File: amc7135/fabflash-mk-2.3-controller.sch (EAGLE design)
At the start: 6 parts, among them U1 Tiny85

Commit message: slowly making progress toward a buildable device
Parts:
- added JP3, JP4, JP5, JP6: M01PTH-0.9MM-NS, A_butts:M01PTH-0.9MM-NS
- JP1, JP2: value (none) -> M01PTH-0.9MM-NS; device A_butts:M05PTH -> A_butts:M01PTH-0.9MM-NS
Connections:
- net 5V: now also JP6.1; no longer JP1.4, JP2.4
- net BLUEPWM: now also JP4.1; no longer JP1.2
- net GND: now also JP3.1; no longer JP1.1, JP1.5, JP2.1, JP2.5
- net GREENPWM: now also JP1.1; no longer JP2.2
- net REDPWM: now also JP2.1; no longer JP2.3
- net WHITEPWM: now also JP5.1; no longer JP1.3
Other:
- moved on the sheet: C1, R1, S1, U1

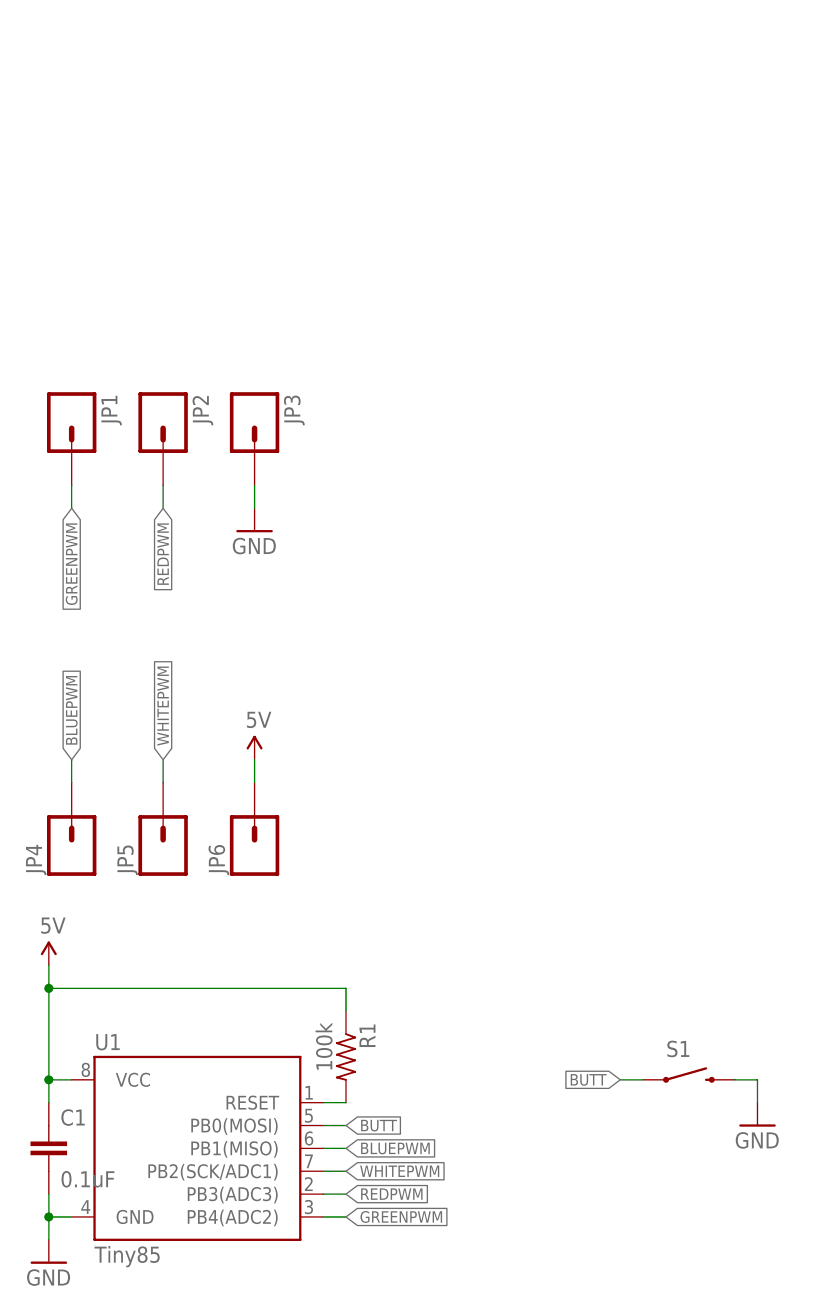
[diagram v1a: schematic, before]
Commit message: batt con plate to smd, controller with isp using jst-zh con
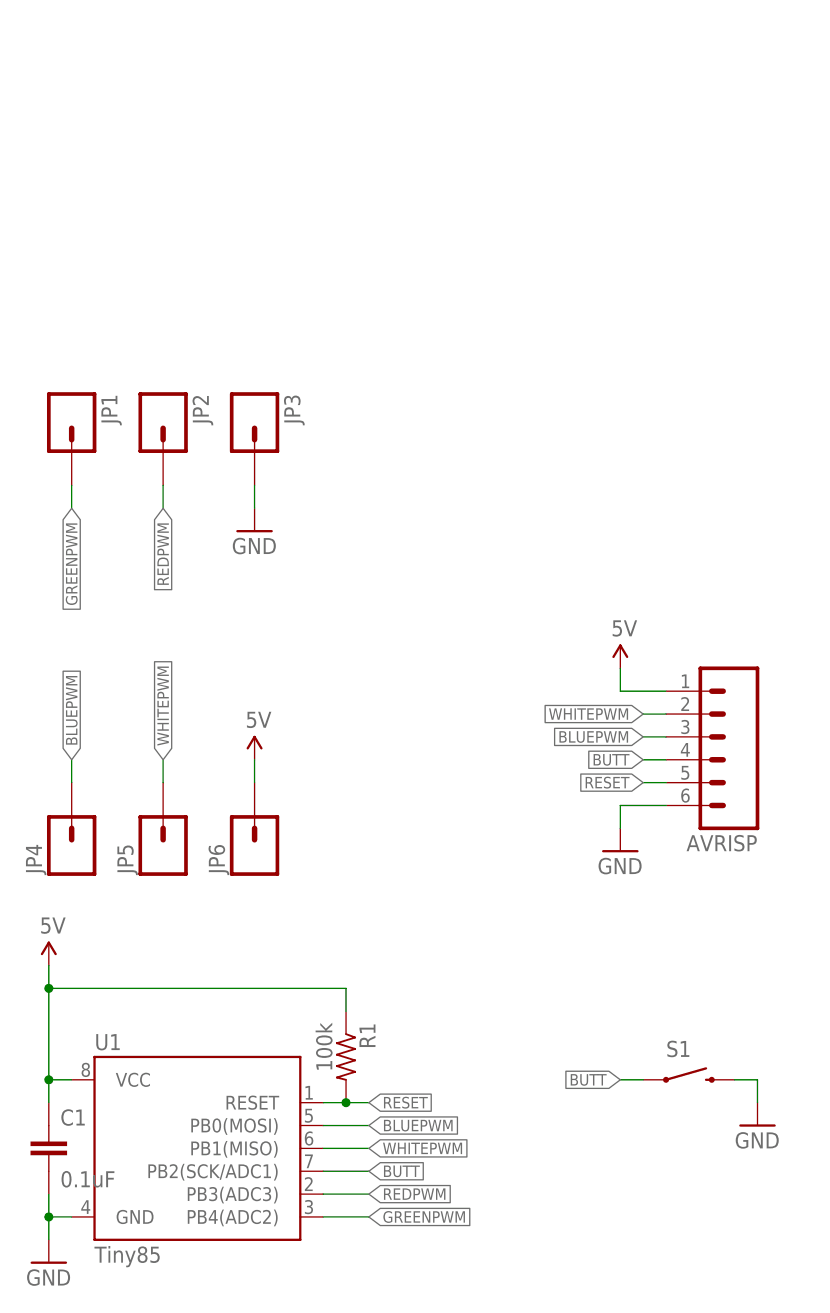
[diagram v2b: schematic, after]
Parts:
- added AVRISP: M06JST-ZH-SMD-RA, A_butts:M06JST-ZH-SMD-RA
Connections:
- removed net N$1: R1.2, U1.RESET
- new net RESET: AVRISP.5, R1.2, U1.RESET
- net 5V: now also AVRISP.1
- net BLUEPWM: now also AVRISP.3, U1.PB0(MOSI); no longer U1.PB1(MISO)
- net BUTT: now also AVRISP.4, U1.PB2(SCK/ADC1); no longer U1.PB0(MOSI)
- net GND: now also AVRISP.6
- net WHITEPWM: now also AVRISP.2, U1.PB1(MISO); no longer U1.PB2(SCK/ADC1)

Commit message: added #2 screw holes to each board and verified pins aligned correctly (had to flipflop 5v/gnd a few times)
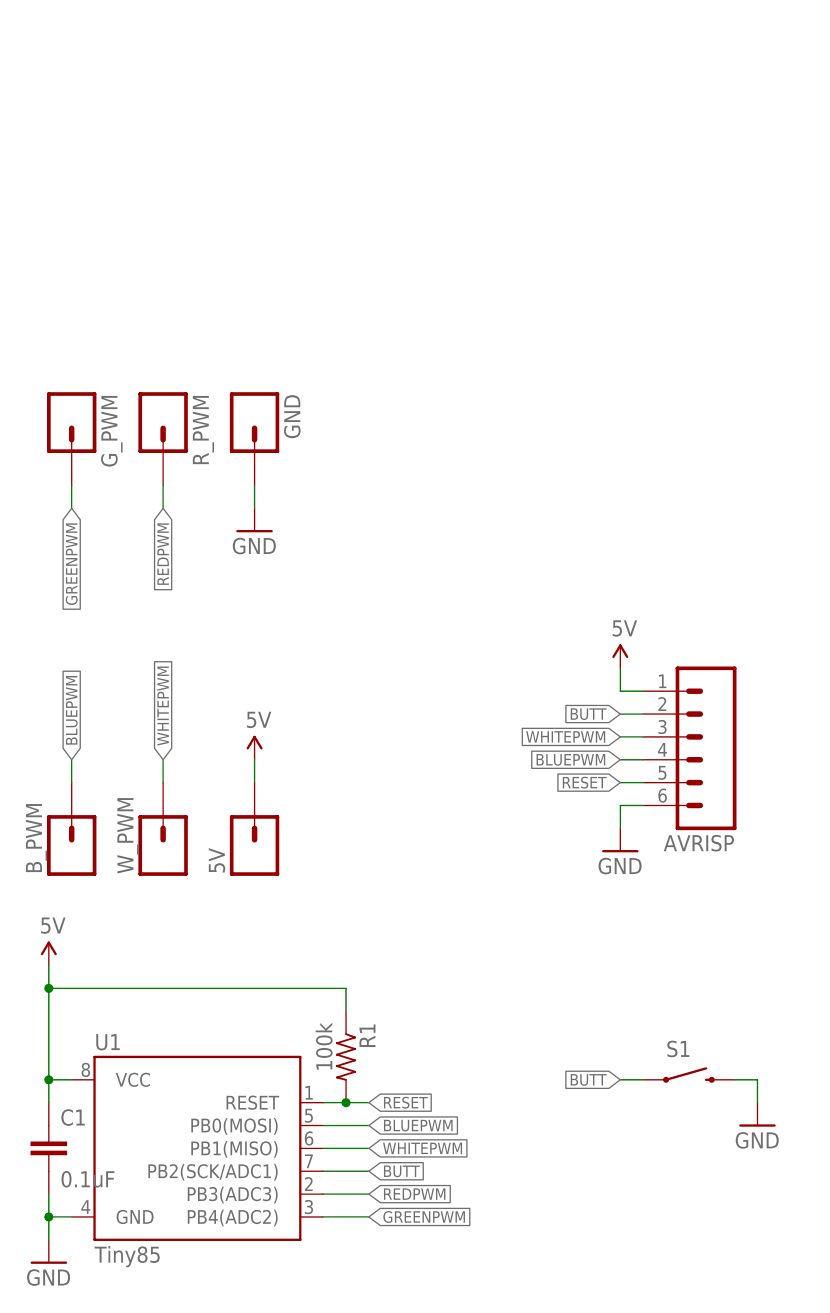
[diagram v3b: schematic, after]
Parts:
- removed JP1, JP2, JP3, JP4, JP5, JP6: M01PTH-0.9MM-NS, A_butts:M01PTH-0.9MM-NS
- added 5V, B_PWM, GND, G_PWM, R_PWM, W_PWM: M01PTH-0.9MM, A_butts:M01PTH-0.9MM
- S1: value SWITCH-MOMENTARY-212MM -> SWITCH-MOMENTARY-2SMD-6MM-GULL; device A_butts:SWITCH-MOMENTARY-212MM -> A_butts:SWITCH-MOMENTARY-2SMD-6MM-GULL
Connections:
- net 5V: now also 5V.1; no longer JP6.1
- net BLUEPWM: now also AVRISP.4, B_PWM.1; no longer AVRISP.3, JP4.1
- net BUTT: now also AVRISP.2; no longer AVRISP.4
- net GND: now also GND.1; no longer JP3.1
- net GREENPWM: now also G_PWM.1; no longer JP1.1
- net REDPWM: now also R_PWM.1; no longer JP2.1
- net WHITEPWM: now also AVRISP.3, W_PWM.1; no longer AVRISP.2, JP5.1
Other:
- moved on the sheet: AVRISP

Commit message: rerouted controller and switched to a jst-ph on top side since bottom side would hit the inductors on the booster board
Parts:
- AVRISP: value M06JST-ZH-SMD-RA -> M06; device A_butts:M06JST-ZH-SMD-RA -> A_butts:M06
- S1: value SWITCH-MOMENTARY-2SMD-6MM-GULL -> SWITCH-MOMENTARY-2PTH; device A_butts:SWITCH-MOMENTARY-2SMD-6MM-GULL -> A_butts:SWITCH-MOMENTARY-2PTH
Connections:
- removed net BLUEPWM: AVRISP.4, B_PWM.1, U1.PB0(MOSI)
- removed net BUTT: AVRISP.2, S1.1, U1.PB2(SCK/ADC1)
- removed net WHITEPWM: AVRISP.3, U1.PB1(MISO), W_PWM.1
- new net MISO: AVRISP.2, U1.PB1(MISO), W_PWM.1
- new net MOSI: AVRISP.3, B_PWM.1, U1.PB0(MOSI)
- new net SCK: AVRISP.4, S1.1, U1.PB2(SCK/ADC1)
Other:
- moved on the sheet: AVRISP
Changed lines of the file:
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@@
 <grid distance="100" unitdist="mil" unit="mil" style="lines" multiple="1" display="yes" altdistance="1" altunitdist="mm" altunit="mm"/>
 <layers>
-<layer number="1" name="Top" color="4" fill="1" visible="no" active="no"/>
-<layer number="16" name="Bottom" color="1" fill="1" visible="no" active="no"/>
-<layer number="17" name="Pads" color="2" fill="1" visible="no" active="no"/>
-<layer number="18" name="Vias" color="2" fill="1" visible="no" active="no"/>
-<layer number="19" name="Unrouted" color="6" fill="1" visible="no" active="no"/>
-<layer number="20" name="Dimension" color="15" fill="1" visible="no" active="no"/>
-<layer number="21" name="tPlace" color="7" fill="1" visible="no" active="no"/>
-<layer number="22" name="bPlace" color="7" fill="1" visible="no" active="no"/>
-<layer number="23" name="tOrigins" color="15" fill="1" visible="no" active="no"/>
-<layer number="24" name="bOrigins" color="15" fill="1" visible="no" active="no"/>
-<layer number="25" name="tNames" color="7" fill="1" visible="no" active="no"/>
-<layer number="26" name="bNames" color="7" fill="1" visible="no" active="no"/>
-<layer number="27" name="tValues" color="7" fill="1" visible="no" active="no"/>
-<layer number="28" name="bValues" color="7" fill="1" visible="no" active="no"/>
+<layer number="1" name="Top" color="4" fill="1" visible="yes" active="no"/>
+<layer number="16" name="Bottom" color="1" fill="1" visible="yes" active="no"/>
+<layer number="17" name="Pads" color="2" fill="1" visible="yes" active="no"/>
+<layer number="18" name="Vias" color="2" fill="1" visible="yes" active="no"/>
+<layer number="19" name="Unrouted" color="6" fill="1" visible="yes" active="no"/>
+<layer number="20" name="Dimension" color="15" fill="1" visible="yes" active="no"/>
+<layer number="21" name="tPlace" color="7" fill="1" visible="yes" active="no"/>
+<layer number="22" name="bPlace" color="7" fill="1" visible="yes" active="no"/>
+<layer number="23" name="tOrigins" color="15" fill="1" visible="yes" active="no"/>
+<layer number="24" name="bOrigins" color="15" fill="1" visible="yes" active="no"/>
+<layer number="25" name="tNames" color="7" fill="1" visible="yes" active="no"/>
+<layer number="26" name="bNames" color="7" fill="1" visible="yes" active="no"/>
+<layer number="27" name="tValues" color="7" fill="1" visible="yes" active="no"/>
+<layer number="28" name="bValues" color="7" fill="1" visible="yes" active="no"/>
 <layer number="29" name="tStop" color="7" fill="3" visible="no" active="no"/>
 <layer number="30" name="bStop" color="7" fill="6" visible="no" active="no"/>
@@
 <layer number="35" name="tGlue" color="7" fill="4" visible="no" active="no"/>
 <layer number="36" name="bGlue" color="7" fill="5" visible="no" active="no"/>
-<layer number="37" name="tTest" color="7" fill="1" visible="no" active="no"/>
-<layer number="38" name="bTest" color="7" fill="1" visible="no" active="no"/>
+<layer number="37" name="tTest" color="7" fill="1" visible="yes" active="no"/>
+<layer number="38" name="bTest" color="7" fill="1" visible="yes" active="no"/>
 <layer number="39" name="tKeepout" color="4" fill="11" visible="no" active="no"/>
 <layer number="40" name="bKeepout" color="1" fill="11" visible="no" active="no"/>
@@
 <layer number="44" name="Drills" color="7" fill="1" visible="no" active="no"/>
 <layer number="45" name="Holes" color="7" fill="1" visible="no" active="no"/>
-<layer number="46" name="Milling" color="3" fill="1" visible="no" active="no"/>
-<layer number="47" name="Measures" color="7" fill="1" visible="no" active="no"/>
-<layer number="48" name="Document" color="7" fill="1" visible="no" active="no"/>
-<layer number="49" name="Reference" color="7" fill="1" visible="no" active="no"/>
-<layer number="50" name="dxf" color="7" fill="1" visible="no" active="no"/>
-<layer number="51" name="tDocu" color="7" fill="1" visible="no" active="no"/>
-<layer number="52" name="bDocu" color="7" fill="1" visible="no" active="no"/>
-<layer number="53" name="tGND_GNDA" color="7" fill="9" visible="no" active="no"/>
-<layer number="54" name="bGND_GNDA" color="1" fill="9" visible="no" active="no"/>
-<layer number="56" name="wert" color="7" fill="1" visible="no" active="no"/>
-<layer number="57" name="tCAD" color="7" fill="1" visible="no" active="no"/>
+<layer number="46" name="Milling" color="3" fill="1" visible="yes" active="no"/>
+<layer number="47" name="Measures" color="7" fill="1" visible="yes" active="no"/>
+<layer number="48" name="Document" color="7" fill="1" visible="yes" active="no"/>
+<layer number="49" name="Reference" color="7" fill="1" visible="yes" active="no"/>
+<layer number="50" name="dxf" color="7" fill="1" visible="yes" active="no"/>
+<layer number="51" name="tDocu" color="7" fill="1" visible="yes" active="no"/>
+<layer number="52" name="bDocu" color="7" fill="1" visible="yes" active="no"/>
+<layer number="53" name="tGND_GNDA" color="7" fill="9" visible="yes" active="no"/>
+<layer number="54" name="bGND_GNDA" color="1" fill="9" visible="yes" active="no"/>
+<layer number="56" name="wert" color="7" fill="1" visible="yes" active="no"/>
+<layer number="57" name="tCAD" color="7" fill="1" visible="yes" active="no"/>
 <layer number="91" name="Nets" color="2" fill="1" visible="yes" active="yes"/>
 <layer number="92" name="Busses" color="1" fill="1" visible="yes" active="yes"/>
@@
 <part name="GND4" library="A_butts" deviceset="GND" device=""/>
 <part name="U1" library="A_butts" deviceset="ATTINY45" device="TINY85-20-SOICW" value="Tiny85"/>
-<part name="S1" library="A_butts" deviceset="SWITCH-MOMENTARY-2" device="SMD-6MM-GULL" value="SWITCH-MOMENTARY-2SMD-6MM-GULL"/>
+<part name="S1" library="A_butts" deviceset="SWITCH-MOMENTARY-2" device="PTH" value="SWITCH-MOMENTARY-2PTH"/>
 <part name="SUPPLY1" library="A_butts" deviceset="5V" device=""/>
 <part name="GND3" library="A_butts" deviceset="GND" device=""/>
@@
 <part name="GND" library="A_butts" deviceset="M01" device="PTH-0.9MM" value="M01PTH-0.9MM"/>
 <part name="B_PWM" library="A_butts" deviceset="M01" device="PTH-0.9MM" value="M01PTH-0.9MM"/>
-<part name="AVRISP" library="A_butts" deviceset="M06" device="JST-ZH-SMD-RA" value="M06JST-ZH-SMD-RA"/>
+<part name="AVRISP" library="A_butts" deviceset="M06" device="" value="M06"/>
 <part name="SUPPLY2" library="A_butts" deviceset="5V" device=""/>
 <part name="GND2" library="A_butts" deviceset="GND" device=""/>
@@
 </segment>
 </net>
-<net name="WHITEPWM" class="0">
+<net name="MISO" class="0">
 <segment>
 <wire x1="20.32" y1="58.42" x2="20.32" y2="60.96" width="0.1524" layer="91"/>
@@
 </segment>
 <segment>
-<pinref part="AVRISP" gate="G$1" pin="3"/>
-<wire x1="73.66" y1="63.5" x2="71.12" y2="63.5" width="0.1524" layer="91"/>
-<label x="71.12" y="63.5" size="1.27" layer="95" rot="R180" xref="yes"/>
+<pinref part="AVRISP" gate="G$1" pin="2"/>
+<wire x1="73.66" y1="66.04" x2="71.12" y2="66.04" width="0.1524" layer="91"/>
+<label x="71.12" y="66.04" size="1.27" layer="95" rot="R180" xref="yes"/>
 </segment>
 </net>
@@
 </segment>
 </net>
-<net name="BUTT" class="0">
+<net name="SCK" class="0">
 <segment>
 <pinref part="S1" gate="G$1" pin="1"/>
@@
 </segment>
 <segment>
-<pinref part="AVRISP" gate="G$1" pin="2"/>
-<wire x1="73.66" y1="66.04" x2="71.12" y2="66.04" width="0.1524" layer="91"/>
-<label x="71.12" y="66.04" size="1.27" layer="95" rot="R180" xref="yes"/>
-</segment>
-</net>
-<net name="BLUEPWM" class="0">
+<pinref part="AVRISP" gate="G$1" pin="4"/>
+<wire x1="73.66" y1="60.96" x2="71.12" y2="60.96" width="0.1524" layer="91"/>
+<label x="71.12" y="60.96" size="1.27" layer="95" rot="R180" xref="yes"/>
+</segment>
+</net>
+<net name="MOSI" class="0">
 <segment>
 <wire x1="10.16" y1="58.42" x2="10.16" y2="60.96" width="0.1524" layer="91"/>
@@
 </segment>
 <segment>
-<pinref part="AVRISP" gate="G$1" pin="4"/>
-<wire x1="73.66" y1="60.96" x2="71.12" y2="60.96" width="0.1524" layer="91"/>
-<label x="71.12" y="60.96" size="1.27" layer="95" rot="R180" xref="yes"/>
-</segment>
-</net>
+<pinref part="AVRISP" gate="G$1" pin="3"/>
+<wire x1="73.66" y1="63.5" x2="71.12" y2="63.5" width="0.1524" layer="91"/>
+<label x="71.12" y="63.5" size="1.27" layer="95" rot="R180" xref="yes"/>
+</segment>
+</net>

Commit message: updating corners to 2mm curve and smoothed out curves on booster pcb
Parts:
- AVRISP: value M06 -> M06PTH-2MM-NS; device A_butts:M06 -> A_butts:M06PTH-2MM-NS
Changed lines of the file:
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@@
 <part name="GND" library="A_butts" deviceset="M01" device="PTH-0.9MM" value="M01PTH-0.9MM"/>
 <part name="B_PWM" library="A_butts" deviceset="M01" device="PTH-0.9MM" value="M01PTH-0.9MM"/>
-<part name="AVRISP" library="A_butts" deviceset="M06" device="" value="M06"/>
+<part name="AVRISP" library="A_butts" deviceset="M06" device="PTH-2MM-NS" value="M06PTH-2MM-NS"/>
 <part name="SUPPLY2" library="A_butts" deviceset="5V" device=""/>
 <part name="GND2" library="A_butts" deviceset="GND" device=""/>
